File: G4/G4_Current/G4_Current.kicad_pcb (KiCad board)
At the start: 2 copper layers, 70.5 x 91.4 mm, 26 parts, among them J1 Conn_01x06_Socket, J2 Conn_01x06_Socket, U1 NUCLEO-G491RE, U2 INA3221_Module, U3 INA3221_Module

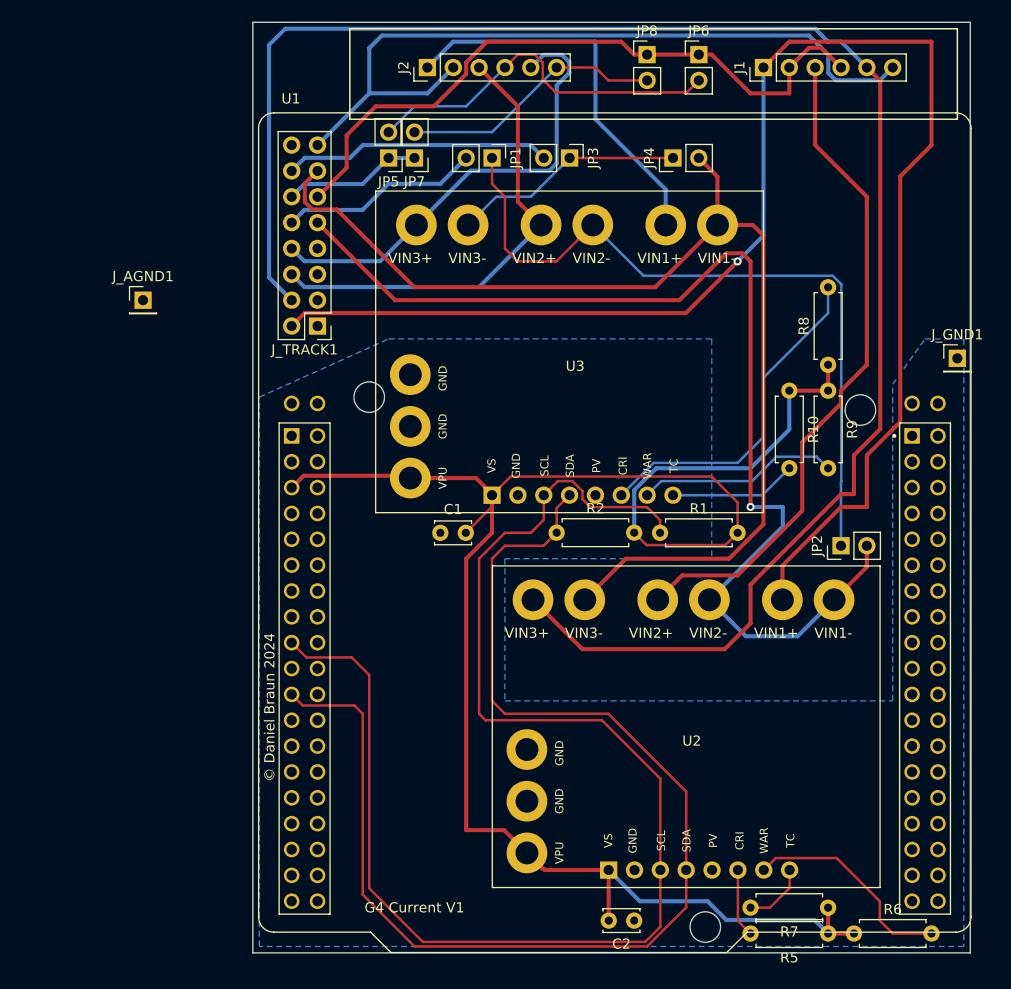
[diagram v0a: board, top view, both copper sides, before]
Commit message: change i2c1 and i2c3 for better routing
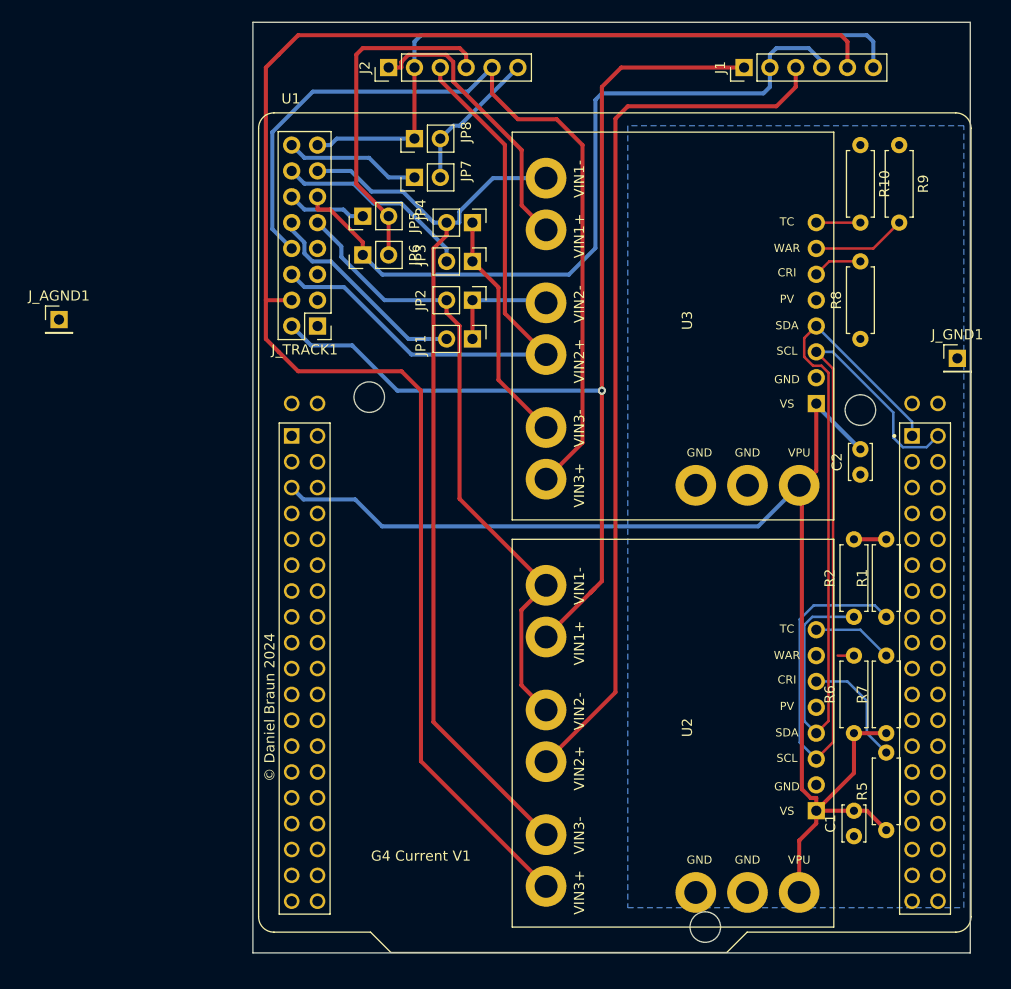
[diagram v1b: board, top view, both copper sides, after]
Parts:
- moved C1 50.4 mm to (151.1, 123.8), turned to 90 degrees
- moved C2 49.1 mm to (151.8, 88.3), turned to 90 degrees
- moved JP2 43.5 mm to (113.6, 71.1), turned to -90 degrees
- moved JP6 38.4 mm to (102.9, 66.7), turned to 90 degrees
- moved U3 33.1 mm to (147.4, 81.3), turned to -90 degrees
- moved R2 30.4 mm to (151.1, 102.2), turned to 90 degrees
- moved R10 25.1 mm to (151.8, 55.9)
- moved R9 25.1 mm to (155.6, 55.9)
- moved JP8 24.3 mm to (108.0, 55.2), turned to 90 degrees
- moved R1 23.7 mm to (154.3, 102.2), turned to 90 degrees
- moved U2 21.2 mm to (147.4, 121.3), turned to -90 degrees
- moved JP4 20.7 mm to (113.6, 63.5), turned to -90 degrees
- moved R6 19.7 mm to (151.1, 113.7), turned to 90 degrees
- moved R7 18.1 mm to (154.3, 113.7), turned to 90 degrees
- moved JP1 17.9 mm to (113.6, 74.9)
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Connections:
- JP7 pad 1: C2B -> C3B
- JP8 pad 1: C0B -> C1B
- R1 pad 1: I2C1_SCL -> I2C3_SCL
- R2 pad 1: I2C1_SDA -> I2C3_SDA
- U2 pad 3: I2C1_SCL -> I2C3_SCL
- U2 pad 4: I2C1_SDA -> I2C3_SDA
- U3 pad 3: I2C1_SCL -> I2C3_SCL
- U3 pad 4: I2C1_SDA -> I2C3_SDA
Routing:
- net I2C1_SCL: track 137.2 -> 0.00 mm
- net I2C1_SDA: track 120.8 -> 0.00 mm
- net I2C3_SCL: track 0.00 -> 83.0 mm
- net I2C3_SDA: track 0.00 -> 73.5 mm
- net Net-(JP1-A): track 72.6 -> 11.2 mm
- net 3V3: track 181.7 -> 133.1 mm
- net C0A: track 110.0 -> 62.8 mm, vias 1 -> 0
- net T00A: track 146.5 -> 104.8 mm
- net T30A_T13A: track 45.6 -> 84.3 mm
- net Net-(U3-CRI): track 33.7 -> 4.86 mm
- net T01A: track 66.1 -> 86.9 mm
- net Net-(U2-WAR): track 21.2 -> 1.60 mm
- net C1A: track 111.4 -> 92.2 mm
- net T20A_T03A: track 45.5 -> 60.8 mm
- net C3B: track 0.00 -> 13.4 mm
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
